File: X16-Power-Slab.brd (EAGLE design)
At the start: 160 x 100 mm, 0 parts

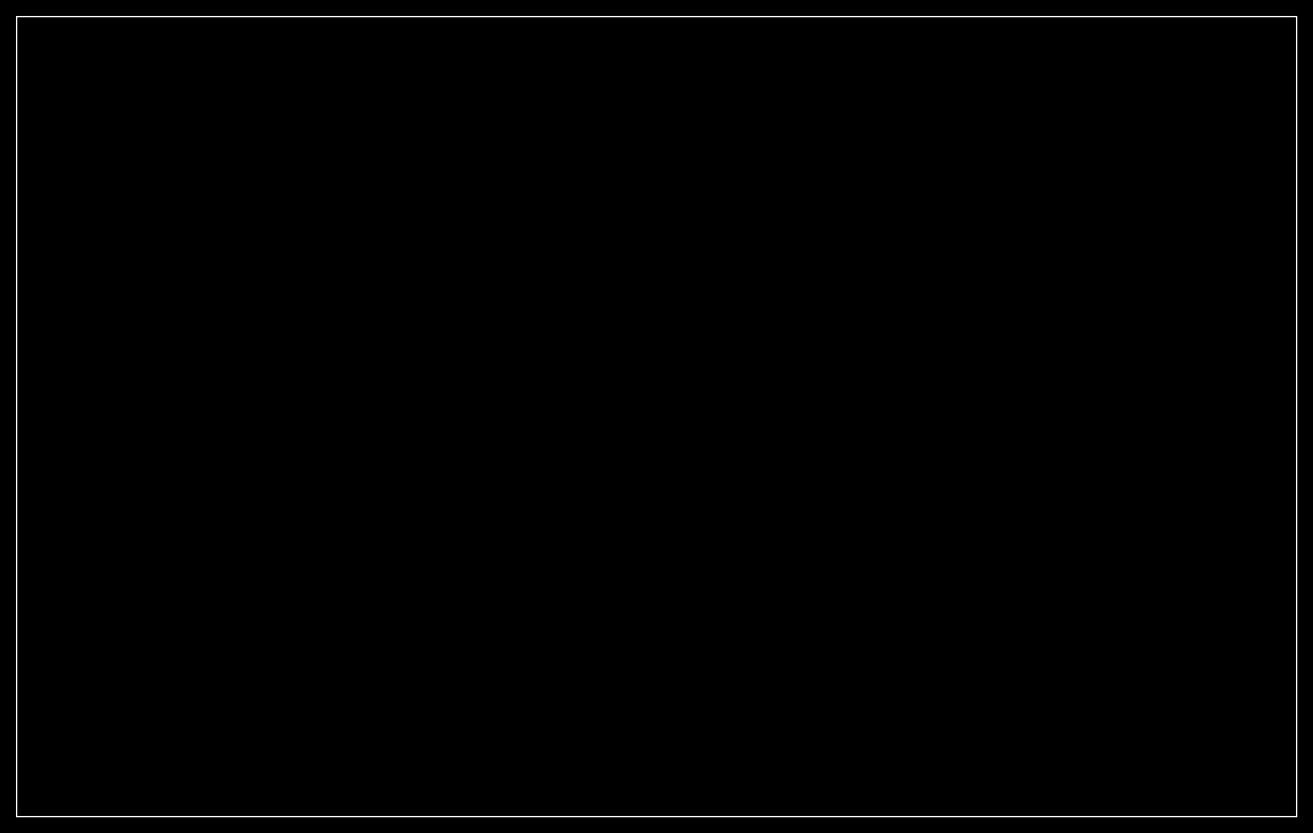
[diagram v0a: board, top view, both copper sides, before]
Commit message: changed dimensions
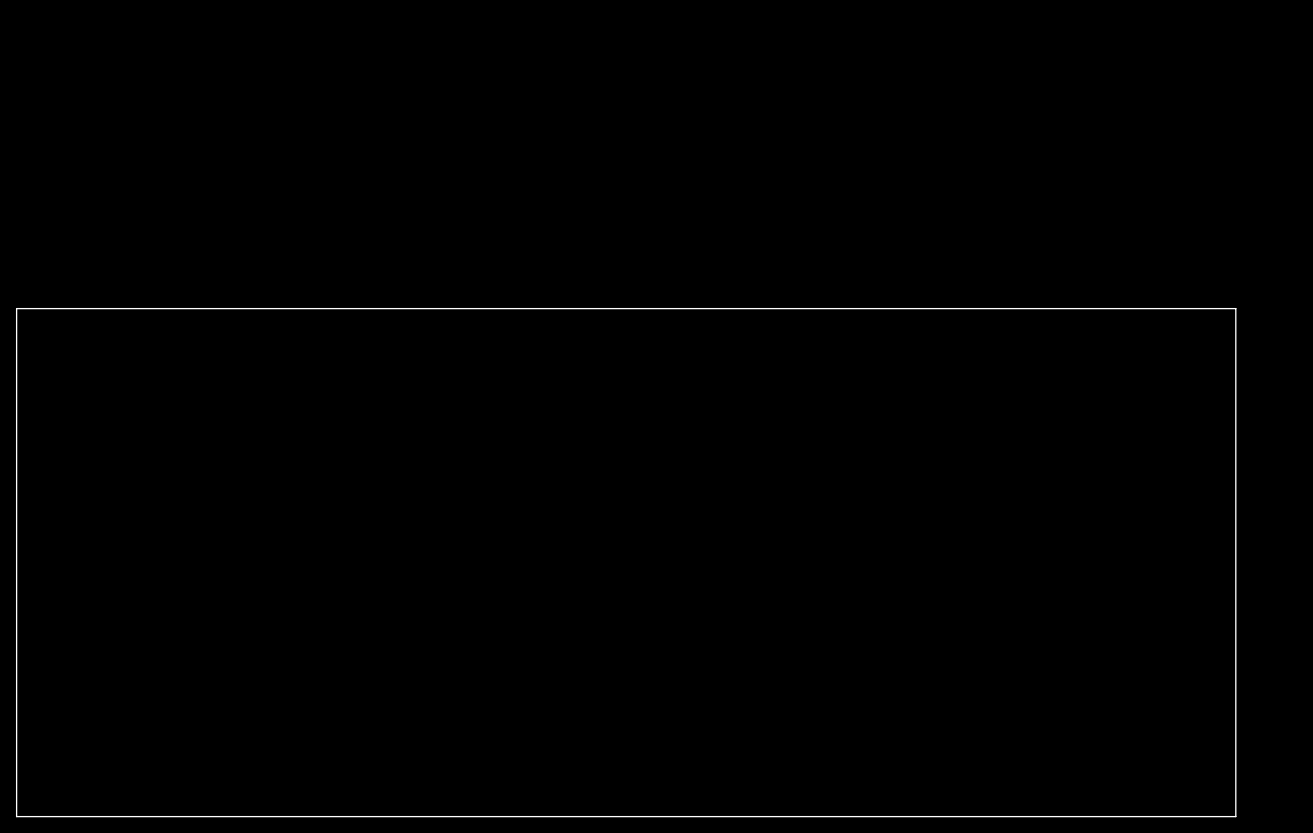
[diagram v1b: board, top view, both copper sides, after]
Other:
- board size 160 x 100 mm -> 152.4 x 63.5 mm
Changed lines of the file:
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@@
 <board>
 <plain>
-<wire x1="0" y1="0" x2="160" y2="0" width="0.1524" layer="20"/>
-<wire x1="0" y1="0" x2="0" y2="100" width="0.1524" layer="20"/>
-<wire x1="160" y1="0" x2="160" y2="100" width="0.1524" layer="20"/>
-<wire x1="160" y1="100" x2="0" y2="100" width="0.1524" layer="20"/>
+<wire x1="0" y1="0" x2="152.4" y2="0" width="0.1524" layer="20"/>
+<wire x1="0" y1="0" x2="0" y2="63.5" width="0.1524" layer="20"/>
+<wire x1="152.4" y1="0" x2="152.4" y2="63.5" width="0.1524" layer="20"/>
+<wire x1="152.4" y1="63.5" x2="0" y2="63.5" width="0.1524" layer="20"/>
 </plain>
 <attributes>

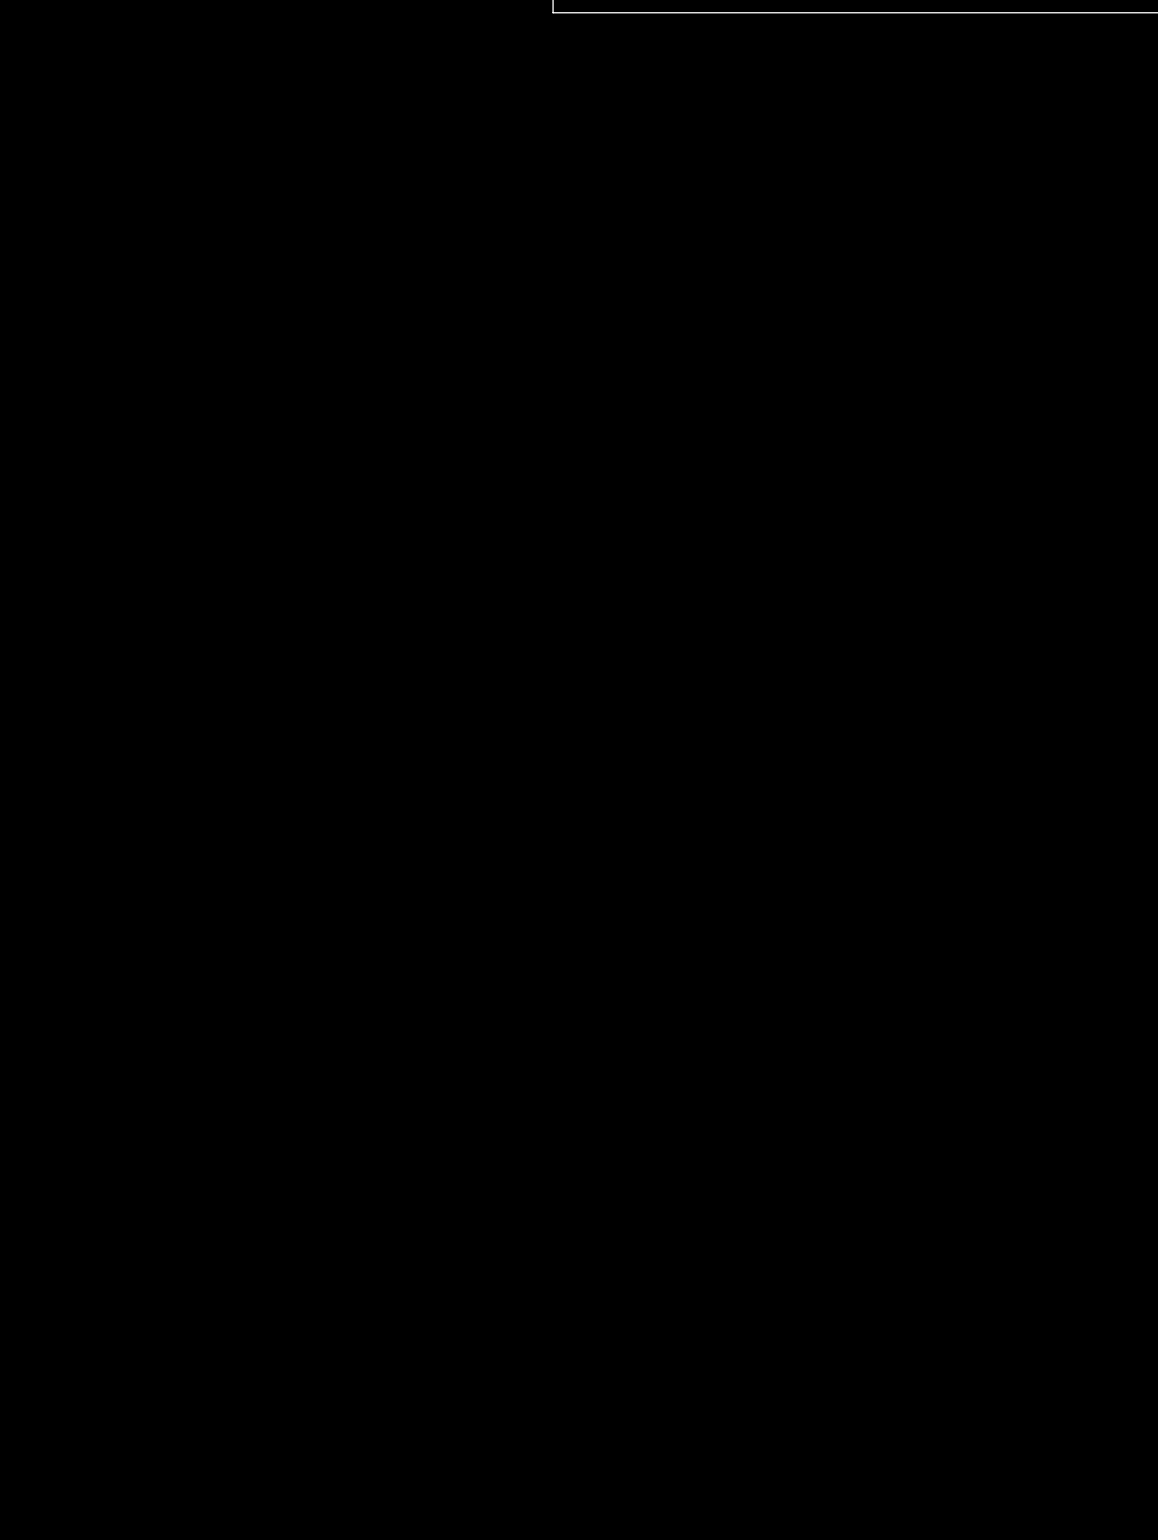
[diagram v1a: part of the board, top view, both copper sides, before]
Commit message: Buck converter added
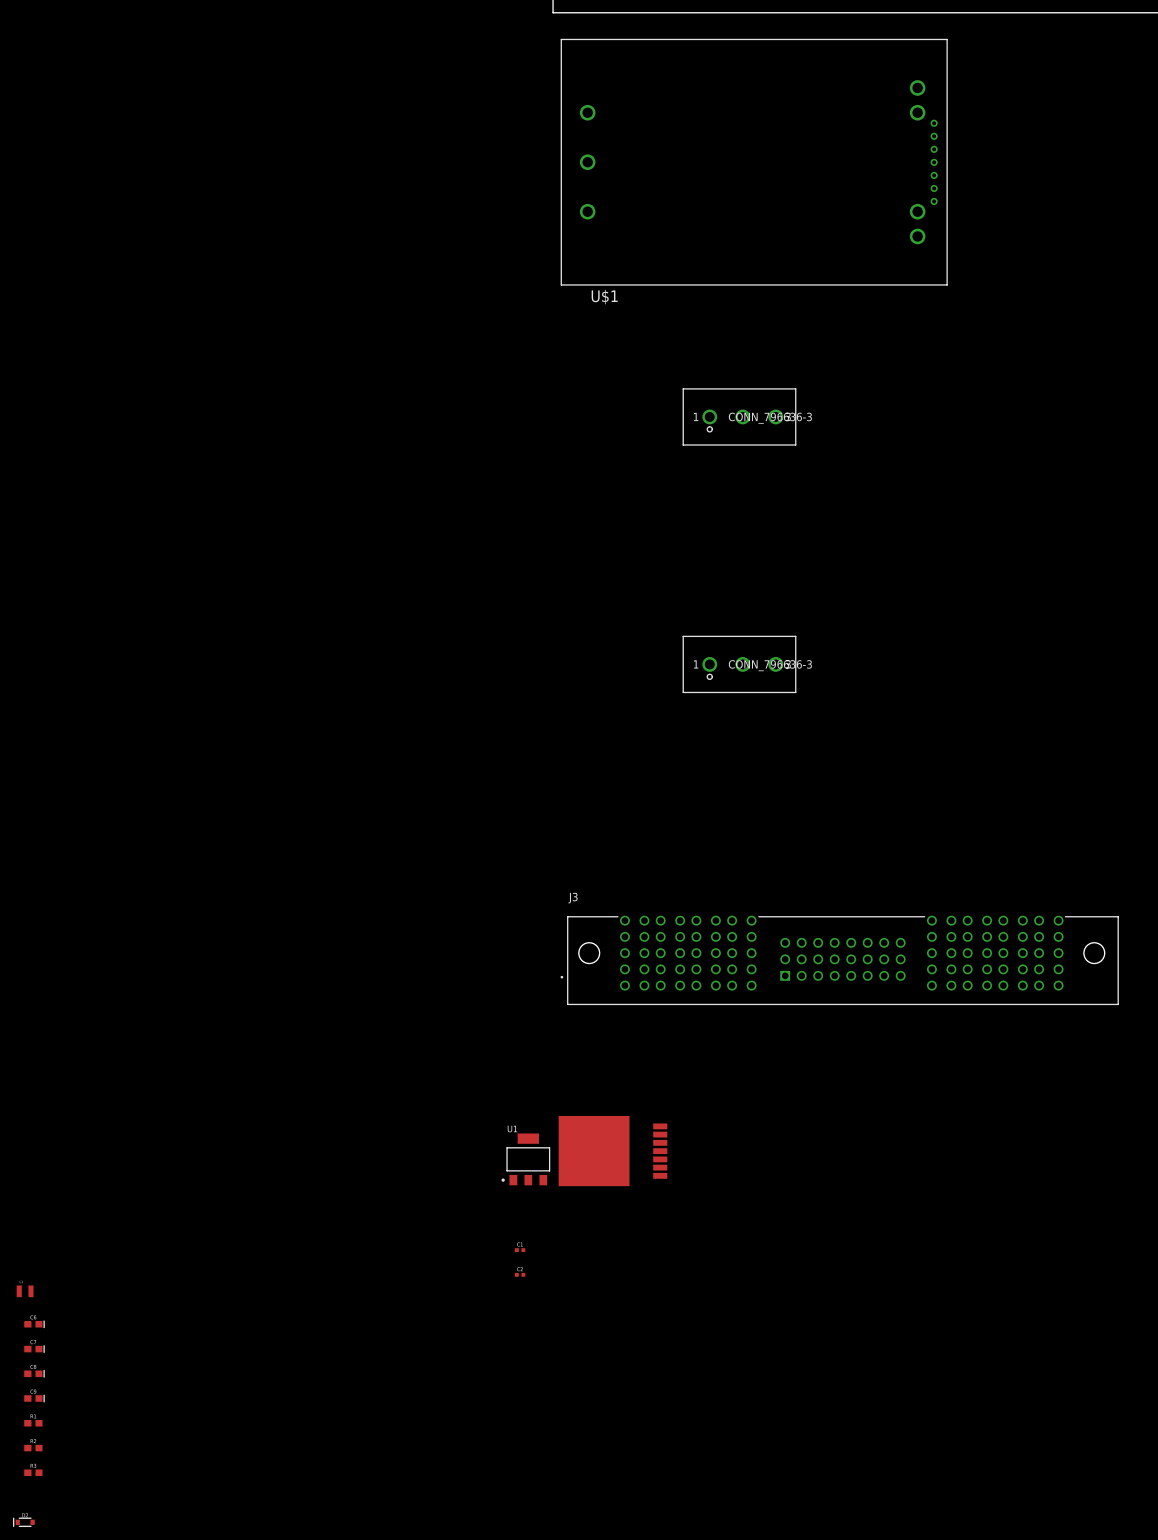
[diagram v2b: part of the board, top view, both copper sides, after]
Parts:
- added C1, C2: 0.5pF, SparkFun-Capacitors:0402-TIGHT
- added C6, C7, C8, C9: 10uF, SparkFun-Capacitors:0603-POLAR
- added D2: 1A/23V/620mV, SparkFun-DiscreteSemi:SOD-323
- added J1, J2: CONN_796636-3, X16_Power_Slab:CONN_796636-3
- added J3: CONN_ET60T, X16_Power_Slab:SAMTEC_ET60T-D04-3-08-D04-X-R1-S
- added L1: 2.2μH_SHIELDED_INDUCTOR, SparkFun-Coils:0806
- added R1, R2, R3: (no value), SparkFun-Resistors:0603
- added U$1: CONN_BMR480_BRICK, X16_Power_Slab:CONN_BMR480_BRICK
- added U$2: BUCK_LM2679SX-ADJ, X16_Power_Slab:BUCK,LM2679SX-ADJ
- added U1: LINEAR_AZ1117CR-3.3TRG1DIODES_AZ1117CH-3.3TRG1_0_0, X16_Power_Slab:LINEAR_AZ1117CR-3.3TRG1
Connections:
- new net 5.2V/2.1A: C6.+, C7.+, C8.+, L1.2, R2.2
- new net GND: R1.2
- new net N$1: C2.1, U$2.PIN3
- new net N$11: C1.2, C6.-, C7.-, C8.-, C9.-, D2.A, R3.1, U$2.PIN4, U$2.PIN8
- new net N$2: C2.2, L1.1, U$2.PIN1
- new net N$4: R1.1, R2.1, U$2.PIN6
- new net N$8: R3.2, U$2.PIN5
- new net N$9: C1.1, C9.+, U$2.PIN2
- new net P01: J3.P01_1, J3.P01_10, J3.P01_2, J3.P01_3, J3.P01_4, J3.P01_5, J3.P01_6, J3.P01_7, J3.P01_8, J3.P01_9
- new net P02: J3.P02_1, J3.P02_10, J3.P02_2, J3.P02_3, J3.P02_4, J3.P02_5, J3.P02_6, J3.P02_7, J3.P02_8, J3.P02_9
- new net P03: J3.P03_1, J3.P03_10, J3.P03_2, J3.P03_3, J3.P03_4, J3.P03_5, J3.P03_6, J3.P03_7, J3.P03_8, J3.P03_9
- new net P04: J3.P04_1, J3.P04_10, J3.P04_2, J3.P04_3, J3.P04_4, J3.P04_5, J3.P04_6, J3.P04_7, J3.P04_8, J3.P04_9
- new net P05: J3.P05_1, J3.P05_10, J3.P05_2, J3.P05_3, J3.P05_4, J3.P05_5, J3.P05_6, J3.P05_7, J3.P05_8, J3.P05_9
- new net P06: J3.P06_1, J3.P06_10, J3.P06_2, J3.P06_3, J3.P06_4, J3.P06_5, J3.P06_6, J3.P06_7, J3.P06_8, J3.P06_9
- new net P07: J3.P07_1, J3.P07_10, J3.P07_2, J3.P07_3, J3.P07_4, J3.P07_5, J3.P07_6, J3.P07_7, J3.P07_8, J3.P07_9
- new net P08: J3.P08_1, J3.P08_10, J3.P08_2, J3.P08_3, J3.P08_4, J3.P08_5, J3.P08_6, J3.P08_7, J3.P08_8, J3.P08_9

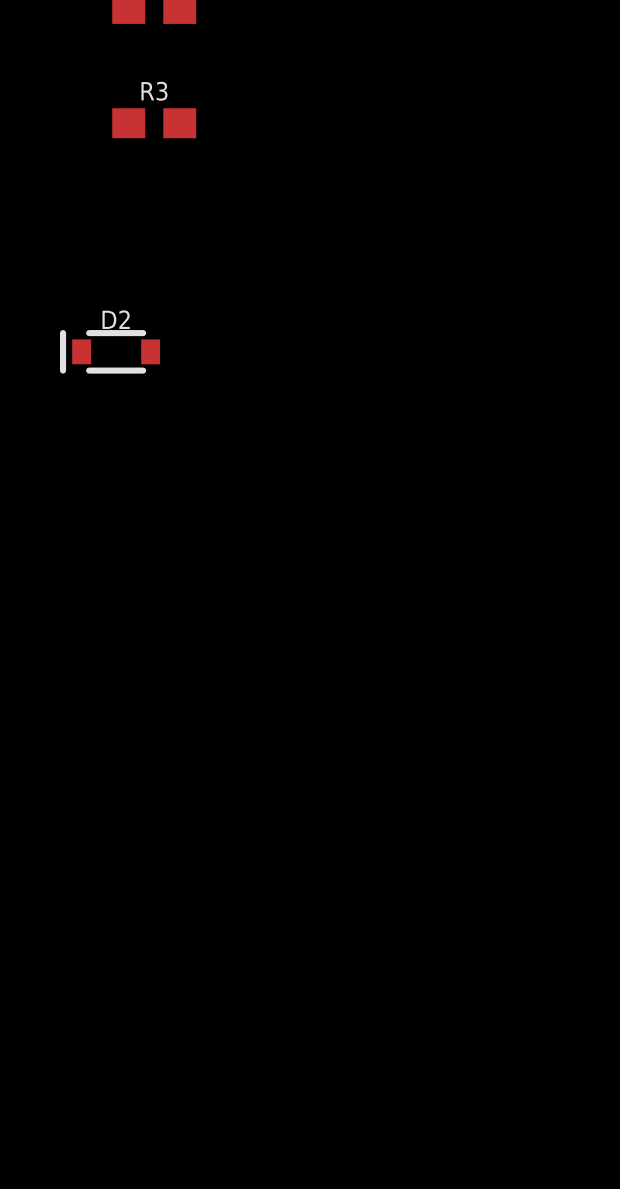
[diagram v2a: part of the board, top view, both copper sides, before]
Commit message: Power Conversion finished, updated Brickstribution
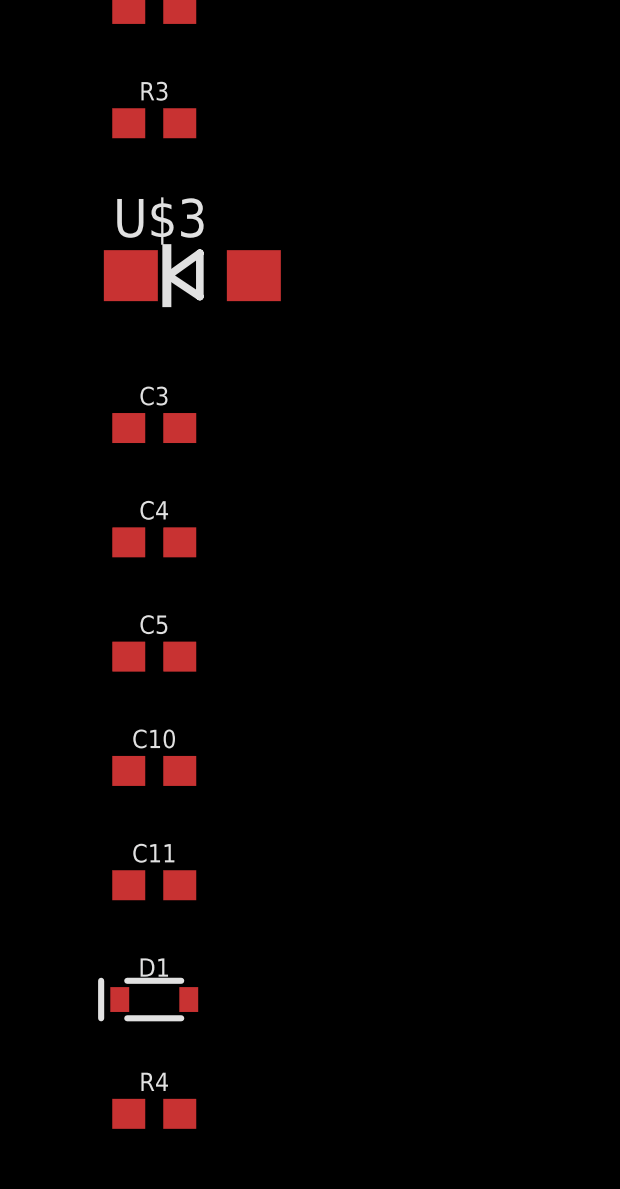
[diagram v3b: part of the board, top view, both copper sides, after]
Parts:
- removed D2: 1A/23V/620mV, SparkFun-DiscreteSemi:SOD-323
- added C10, C11, C3, C4, C5: 0.1uF, SparkFun-Capacitors:0603
- added D1: 3.6V, SparkFun-DiscreteSemi:SOD-323
- added R4: (no value), SparkFun-Resistors:0603
- added U$3: CDBG520-G, X15-Conversion-Parts-Library:DO214AC
- R3: value (none) -> 12.4k
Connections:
- net N$9 renamed 12V/2.1A
- new net 48V: J1.1, J1.2, J1.3
- new net GND/2.2D: C1.2, C6.-, C7.-, C8.-, C9.-, R3.1, U$2.PIN4, U$2.PIN8, U$3.A
- new net N$10: U$1.PIN5
- new net N$12: U$1.PIN8
- new net N$13: U$1.PIN7
- new net N$14: U$1.PIN3
- new net N$15: U$1.PIN1
- new net N$16: C10.1, C11.1, C5.1
- new net N$17: C10.2, C11.2, C5.2
- new net N$3: C3.1, U1.3
- new net N$5: U1.1
- new net N$6: C4.1, U1.2, U1.4
- new net N$7: C3.2
- new net N$9: C4.2
- net GND: now also J2.1, J2.2, J2.3
- net N$11: now also U$1.PIN4; no longer C1.2, C6.-, C7.-, C8.-, C9.-, D2.A, R3.1, U$2.PIN4, U$2.PIN8
- net N$2: now also U$3.C
